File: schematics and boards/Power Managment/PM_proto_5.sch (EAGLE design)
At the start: 35 parts, among them P1 BAT-1, P10 SBC-2, P11 MCU-1, P12 MCU-2, P13 MDB-3, P14 MDB-4, P15 ES-1, P16 ES-2, P17 SIG1, P18 SIG2, P2 BAT-2, P3 SW-1, P4 SW-2, P5 SW-3, P6 SW-4, P7 MDB-1, P8 MDB-2, P9 SBC-1, U1 L78S10CV, U2 L78S05CV

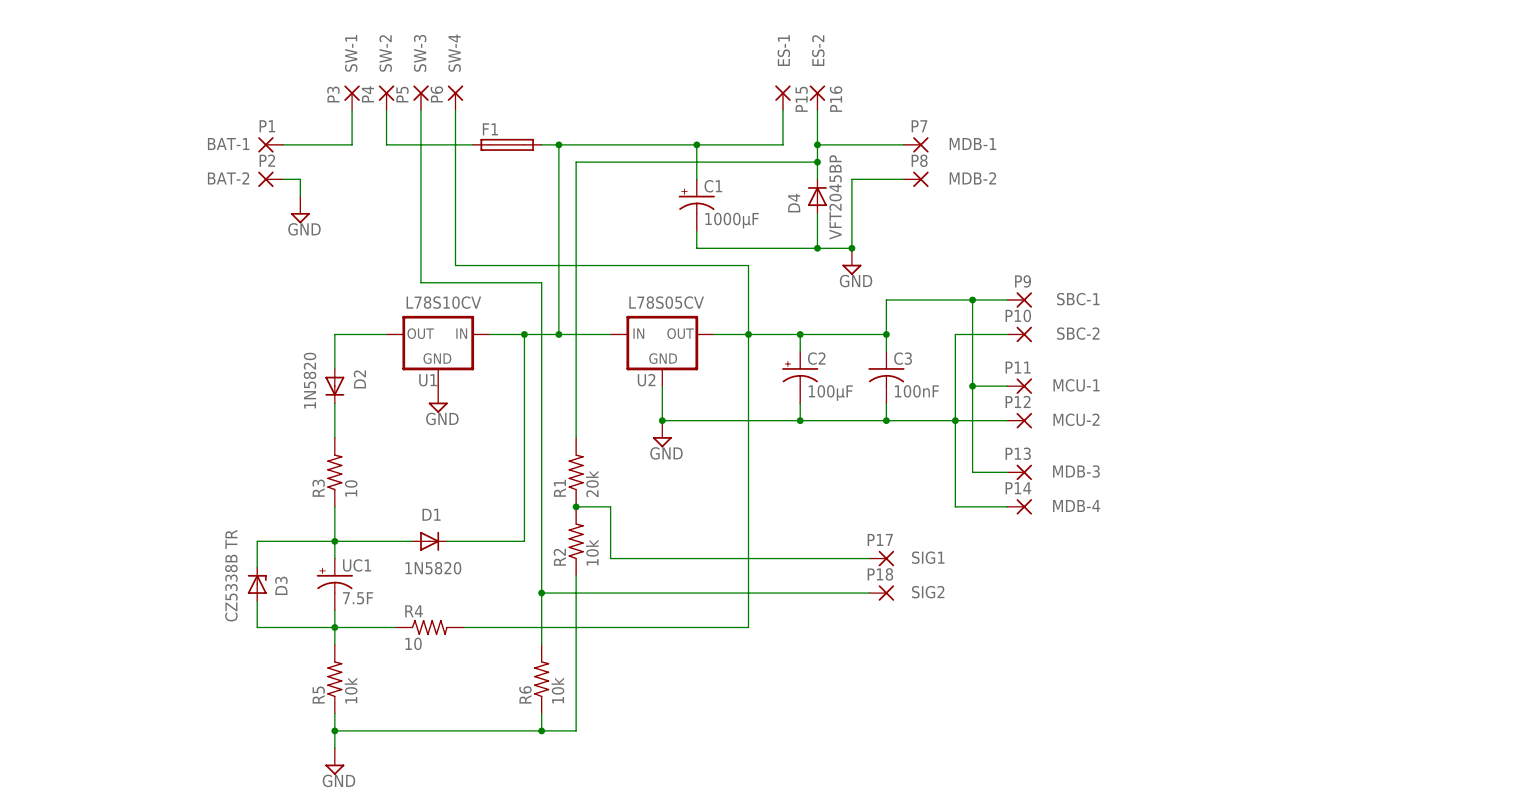
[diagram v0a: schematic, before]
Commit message: Made a small change in the Power Distribution board within the new 5th version. Cleaned up the schematic names and got rid of outdated or useless schematic and board files.
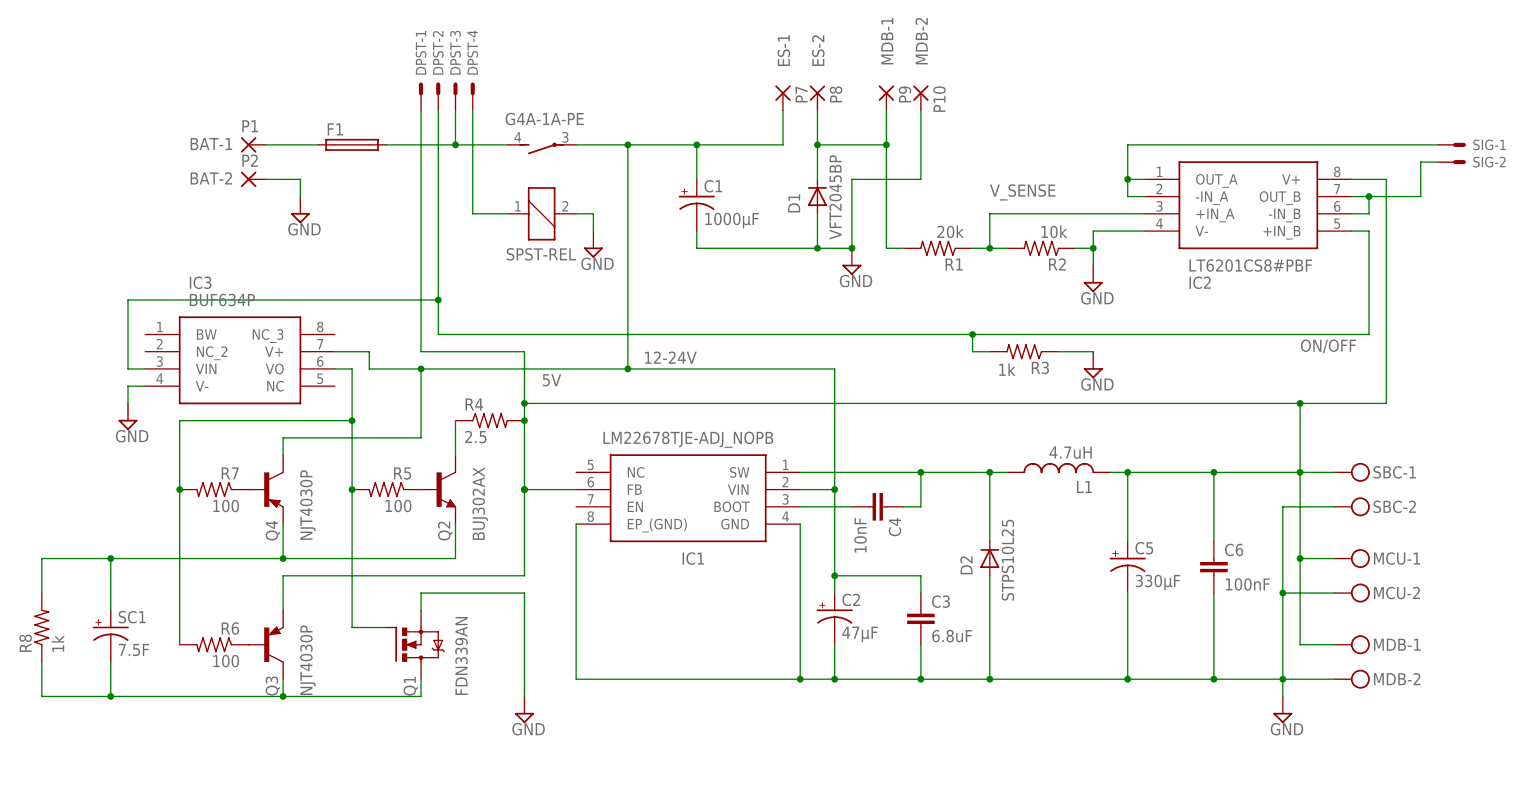
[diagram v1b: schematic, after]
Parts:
- removed D3: CZ5338B TR, diode:1N4728
- removed D4: VFT2045BP, rasm_parts:VFT2045BP
- removed P11: MCU-1, wirepad:1,6/0,8
- removed P12: MCU-2, wirepad:1,6/0,8
- removed P13: MDB-3, wirepad:1,6/0,8
- removed P14: MDB-4, wirepad:1,6/0,8
- removed P15: ES-1, wirepad:1,6/0,8
- removed P16: ES-2, wirepad:1,6/0,8
- removed P17: SIG1, wirepad:1,6/0,8
- removed P18: SIG2, wirepad:1,6/0,8
- removed P3: SW-1, wirepad:1,6/0,8
- removed P4: SW-2, wirepad:1,6/0,8
- removed P5: SW-3, wirepad:1,6/0,8
- removed P6: SW-4, wirepad:1,6/0,8
- removed U1: L78S10CV, v-reg:78XXS
- removed U2: L78S05CV, v-reg:78XXS
- removed UC1: 7.5F, rasm_parts:SCMT32D755MRBB0
- added C4: 10nF, rcl:C-EU025-024X044
- added C5: 330μF, rcl:CPOL-USE2,5-6E
- added C6: 100nF, rcl:C-EU025-024X044
- added DPST: JST-XH-04-PIN-LONG-PAD, Rembrandt Electronics - JST XH Connectors v1-0:JST-XH-04-PIN-LONG-PAD
- added IC1: LM22678TJE-ADJ_NOPB, rasm-other:LM22678TJE-ADJ_NOPB
- added IC2: LT6201CS8#PBF, rasm-other:LT6201CS8#PBF
- added IC3: BUF634P, ic:BUF634P
- added L1: 4.7uH, rcl:L-US6000-XXX-RC
- added MCU, MDB, SBC: MKDSN1,5/2-5,08, con-phoenix-508:MKDSN1,5/2-5,08
- added Q1: FDN339AN, transistor-power:IRFZ48Z
- added Q2: BUJ302AX, transistor:2N706
- added Q3, Q4: NJT4030P, transistor:BC177B-PNP-TO18-EBC
- added R7: 100, rcl:R-US_0204/7
- added R8: 1k, rcl:R-US_0204/7
- added SC1: 7.5F, rasm_parts:SCMT32D755MRBB0
- added SIG: JST-XH-02-PIN-LONG-PAD, Rembrandt Electronics - JST XH Connectors v1-0:JST-XH-02-PIN-LONG-PAD
- added SPST-REL: G4A-1A-PE, rasm-other:G4A-1A-PE
- C2: value 100μF -> 47μF
- C3: value 100nF -> 6.8uF; device rcl:C-US050-024X044 -> rcl:C-EU025-024X044
- D1: value 1N5820 -> VFT2045BP; device diode:1N4004 -> rasm_parts:VFT2045BP
- D2: value 1N5820 -> STPS10L25; device diode:1N4004 -> rasm_parts:VFT2045BP
- P10: value SBC-2 -> MDB-2
- P7: value MDB-1 -> ES-1
- P8: value MDB-2 -> ES-2
- P9: value SBC-1 -> MDB-1
- R3: value 10 -> 1k; device rasm_parts:TNP10SC10R0FE -> rcl:R-US_0204/7
- R4: value 10 -> 2.5
- R5, R6: value 10k -> 100
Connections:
- removed net 5VPWR: C2.+, C3.1, P11.P, P13.P, P6.P, P9.P, R4.2, U2.OUT
- removed net BATT_2: F1.1, P4.P
- removed net BATT_3: C1.+, D1.C, F1.2, P15.P, U1.IN, U2.IN
- removed net CAP_NEG: D3.A, R4.1, R5.2, UC1.-
- removed net CAP_POS: D1.A, D3.C, R3.1, UC1.+
- removed net ON_SENSE: P18.P, P5.P, R6.2
- new net 12-24V: C1.+, C2.+, C3.1, IC1.VIN, IC3.V+, P7.P, Q4.C, SPST-RELG$2.P
- new net 5V: C5.+, C6.1, DPST-1.S, IC1.FB, IC2.V+, L1.2, MCU-1.KL, MDB-1.KL, Q3.E, R4.2, SBC-1.KL
- new net N$1: C4.2, IC1.BOOT
- new net N$10: Q1.D, Q3.C, R8.1, SC1.-
- new net N$11: IC2.-IN_B, IC2.OUT_B, SIG-2.S
- new net N$12: IC2.-IN_A, IC2.OUT_A, SIG-1.S
- new net N$13: DPST-3.S, F1.2, SPST-RELG$2.S
- new net N$14: DPST-4.S, SPST-RELG$1.1
- new net N$4: C4.1, D2.C, IC1.SW, L1.1
- new net N$5: Q4.B, R7.1
- new net N$6: Q2.E, Q4.E, R8.2, SC1.+
- new net N$7: Q3.B, R6.1
- new net N$8: Q2.B, R5.1
- new net ON/OFF: DPST-2.S, IC2.+IN_B, IC3.VIN, R3.2
- net BATT_1: now also F1.1; no longer P3.P
- net BATT_4: now also D1.C, P8.P, P9.P; no longer D4.C, P16.P, P7.P
- net GND: now also C5.-, C6.2, D1.A, D2.A, IC1.EP_(GND), IC1.GND, IC2.V-, IC3.V-, MCU-2.KL, MDB-2.KL, Q1.S, R3.1, SBC-2.KL, SPST-RELG$1.2; no longer D4.A, P12.P, P14.P, P8.P, R5.1, R6.1, U1.GND, U2.GND
- net N$2: now also IC3.VO, Q1.G, R5.2, R6.2, R7.2; no longer D2.A, U1.OUT
- net N$3: now also Q2.C, R4.1; no longer D2.C, R3.2
- net V_SENSE: now also IC2.+IN_A; no longer P17.P
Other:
- moved on the sheet: C2, C3, F1, P1, P10, P2, P7, P8, P9, R1, R2, R3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
